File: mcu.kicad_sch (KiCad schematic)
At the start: 46 parts, among them J10 SWD, Cortex-M 10-pin 1.27 mm, Q20 2N7002, SW1 RESET (RUN to GND), SW2 BOOTSEL (via R24), U20 RP2354B, Y1 12 MHz ABM8-272-T3, CL 10 pF

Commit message: Schematic review: TPS2121 input stage, DS-009 ports, sequencing and CS fixes; docs trimmed
Datasheet-grounded review of the full flight-controller schematic. Downstream
of the input everything verified pin-by-pin (TPS62913, TPS7A20, RP2354B,
BMI088/BMP581/ADXL375, W25Q128, microSD, PWM). The 5 V input stage did not:

- LM66100 (5.5 V rec-op / 6 V abs-max) replaced by one TPS2121 mux (U25):
  BEC priority on IN1, OV lockout ~5.86 V, current limit ~1.5 A, reverse
  blocking on both inputs, source status on GPIO39. Input spec 4.75-5.5 V.
- 5V_IN: 2x4.7 uF + 100 uF + SMAJ5.0A TVS; J3 JST-XH -> XT30PW-M (pin 1 GND).
- J6/J7/J9 reordered to Pixhawk DS-009 (VCC/sig/sig/GND); GPS/ELRS VCC 5 V.
- VIN_SENSE 22k/10k (full scale 10.6 V, was saturating at 5.5 V).
- TPS7A20 EN <- PWR_GOOD so V3V3_ANA rises after V3V3_SYS.
- RP2354B VREG_AVDD moved to V3V3_SYS (datasheet 6.1.8: must power up with
  VREG_VIN); ADC_AVDD stays on V3V3_ANA.
- 10k pull-ups on the four sensor chip-selects.
- ERC "global label appears once" re-enabled (0 hits).

Generator, netlist checker and SPICE decks updated (TPS2121 behavioral model,
new over-voltage and 2S mis-plug corners). Build idempotent, 143 pin mappings
PASS, ERC 0/0, all corners PASS.

Docs: POWER_*.md history removed, rationale folded into DESIGN_SPEC Decisions;
808 -> 290 lines across README, DESIGN_SPEC, LIBRARIES, simulations/README.

Co-Authored-By: Claude Fable 5.1 <noreply@anthropic.com>
Claude-Session: https://claude.ai/code/session_015cFNiWgf35VN2T43HaK8PE
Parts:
- R27: value 10k / 1%, 5V_IN top -> 22k / 1%, 5V_IN top
- R28: value 15k / 1%, 5V_IN bottom -> 10k / 1%, 5V_IN bottom
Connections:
- net V3V3_ANA: no longer R20.1
- net V3V3_SYS: now also R20.1
- net PWR_SRC_ST: now reaches U20.48 (GPIO39)
- no-connect marks 13 -> 12
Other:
- note added: "Crystal circuit per design guide Sec 4: ABM8-272-T3, 15 pF each side (7.5 pF series + ~3 pF stray = 10.5 pF vs CL 10 pF), 1 k in the XOUT leg to limit drive with a 50 ohm ESR crystal. C38 is the single design-guide decoupling exception (pins 68+69 share it). VREG_AVDD RC = 33 ohm + 4.7 uF (design guide Sec 2.1), taken from V3V3_SYS; VREG_FB is tied to DVDD, VREG_PGND to GND, EP to GND."
- note added: "PORT NAMING: a port label is named for the peripheral pin it comes from, so GPS_TX / ELRS_TX are module outputs and land on MCU UART RX pins, while GPS_RX / ELRS_RX are module inputs fed by the MCU UART TX pins. On J6/J7 (POWER 3, Pixhawk DS-009 order 1 VCC / 2 TX / 3 RX / 4 GND) pin 2 is therefore GPS_RX / ELRS_RX. J6 and J7 VCC are on V5_SYS; J9 VCC stays on V3V3_SYS. All port SIGNAL pins remai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"
- note added: "RP2354B, QFN-80, 2 MB in-package QSPI flash. Digital rails on V3V3_SYS, core DVDD from the on-chip buck. RAIL SPLIT: V3V3_ANA (TPS7A20 LDO) now feeds exactly one RP2354B pin - ADC_AVDD (pin 59, with C40). The core regulator input filter R20/C41 that produces VREG_AVDD is fed from V3V3_SYS instead, so the buck-converter reference current no longer flows out of the low-noise analog rail and the sen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"
- note added: "Telemetry dividers, 100 nF at each ADC pin. VIN_SENSE (R27/R28 22k/10k) scales by 10/32 = 0.3125, so the 3.3 V ADC full scale is 10.56 V: 1.56 V at 5.00 V in, 1.72 V at 5.50 V, and a 2S mis-plug at 8.4 V still reads on-scale (2.63 V) instead of pinning the input, which is the point of the wider divider. VBUS_SENSE keeps 10k/15k. Buzzer runs from V5_SYS (avionics OR output), never from the servo b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"
- note removed: "Crystal circuit per design guide Sec 4: ABM8-272-T3, 15 pF each side (7.5 pF series + ~3 pF stray = 10.5 pF vs CL 10 pF), 1 k in the XOUT leg to limit drive with a 50 ohm ESR crystal. C38 is the single design-guide decoupling exception (pins 68+69 share it). VREG_AVDD RC = 33 ohm + 4.7 uF (design guide Sec 2.1); VREG_FB is tied to DVDD, VREG_PGND to GND, EP (pin 81) to GND."
- note removed: "PORT NAMING: a port label is named for the peripheral pin it comes from, so GPS_TX / ELRS_TX are module outputs and land on MCU UART RX pins, while GPS_RX / ELRS_RX are module inputs fed by the MCU UART TX pins. J6/J7/J9 (POWER 3) are 3.3 V logic powered directly from V3V3_SYS."
- note removed: "RP2354B, QFN-80, 2 MB in-package QSPI flash. Digital rails on V3V3_SYS, analog rails on V3V3_ANA, core DVDD from the on-chip buck. Decoupling, core regulator, crystal and BOOTSEL follow the RP2350 hardware design guide; every pin net is a global label."
- note removed: "Telemetry dividers: 10k/15k gives 3.00 V at 5.00 V in, 3.15 V at 5.25 V; 100 nF at each ADC pin. Buzzer runs from V5_SYS (avionics OR output), never from the servo bus; D22 clamps the coil kick. QSPI_* are the dedicated QSPI pads: they reach the in-package flash die AND the package pins (RP2350 datasheet Sec 14.3), so U24 shares the bus with GPIO0/QMI CS1n (FLASH_CS1) as its select. RP2354 requir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"

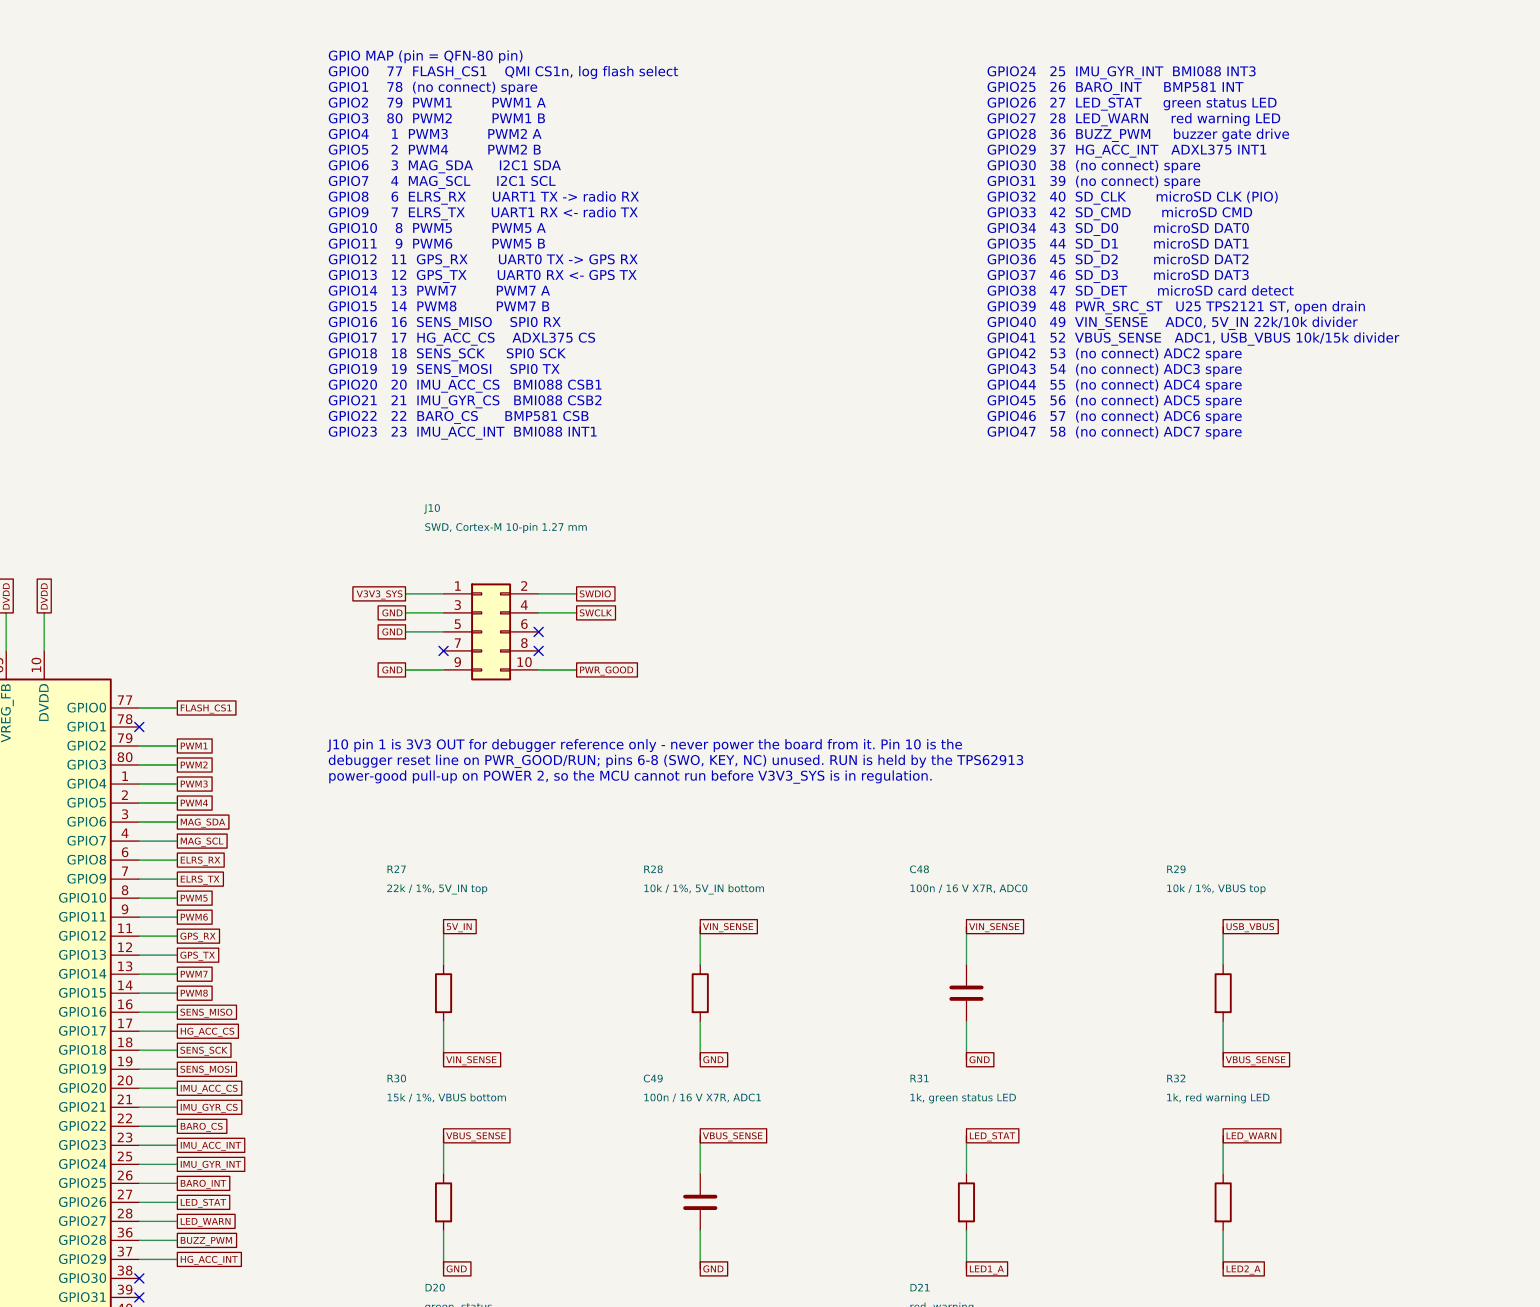
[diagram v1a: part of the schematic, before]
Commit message: Replace BMI088 with ICM-45686; vendor all footprints and 3D models for layout
Sensors: U21 is now the TDK ICM-45686 (single AP_CS on GPIO20 as IMU_CS,
INT1/INT2 on GPIO23/24, GPIO21 spare, R49 dropped, VDD+VDDIO on V3V3_ANA
with 100 nF + 1 uF each). Project-local symbol, footprint and stand-in STEP;
footprint numbering verified against DS-000577 Rev 1.0 Sec 11.2 (CCW, top
view). BMI088_SPI derived-symbol machinery removed from the generator.

Layout readiness: new tools/audit_footprints.py checks every component for
a resolvable footprint and present 3D model (128/128 OK). The seven official
KiCad footprints whose STEP files are absent from kicad-packages3d 10.0.6
are vendored into MARV_Packages.pretty with project-local models in
MARV_Packages.3dshapes: manufacturer STEPs (Coilcraft XGL4030, Molex
104031-0811), EasyEDA model (HRO TYPE-C-31-M-12), FreeCAD-generated bodies
from tools/3d/ (RP2354B QFN-80, TPS62913 RPU0010A, TPS2121 RUX0012A, Amass
XT30PW-M), and KiCad generic stand-ins (BMP581, ADXL375). Model offsets were
derived by measurement and confirmed in a rendered check board.
PROVENANCE.md records source, licence and SHA256 per model; LIBRARIES.md
lists the pre-fab 3D-viewer checks and the unverified dimensions.

Checks: build idempotent, ERC 0/0, check_power_netlist 149 mappings /
128 components, run_power_checks PASS, audit 0 needing action.

Co-Authored-By: Claude Fable 5.1 <noreply@anthropic.com>
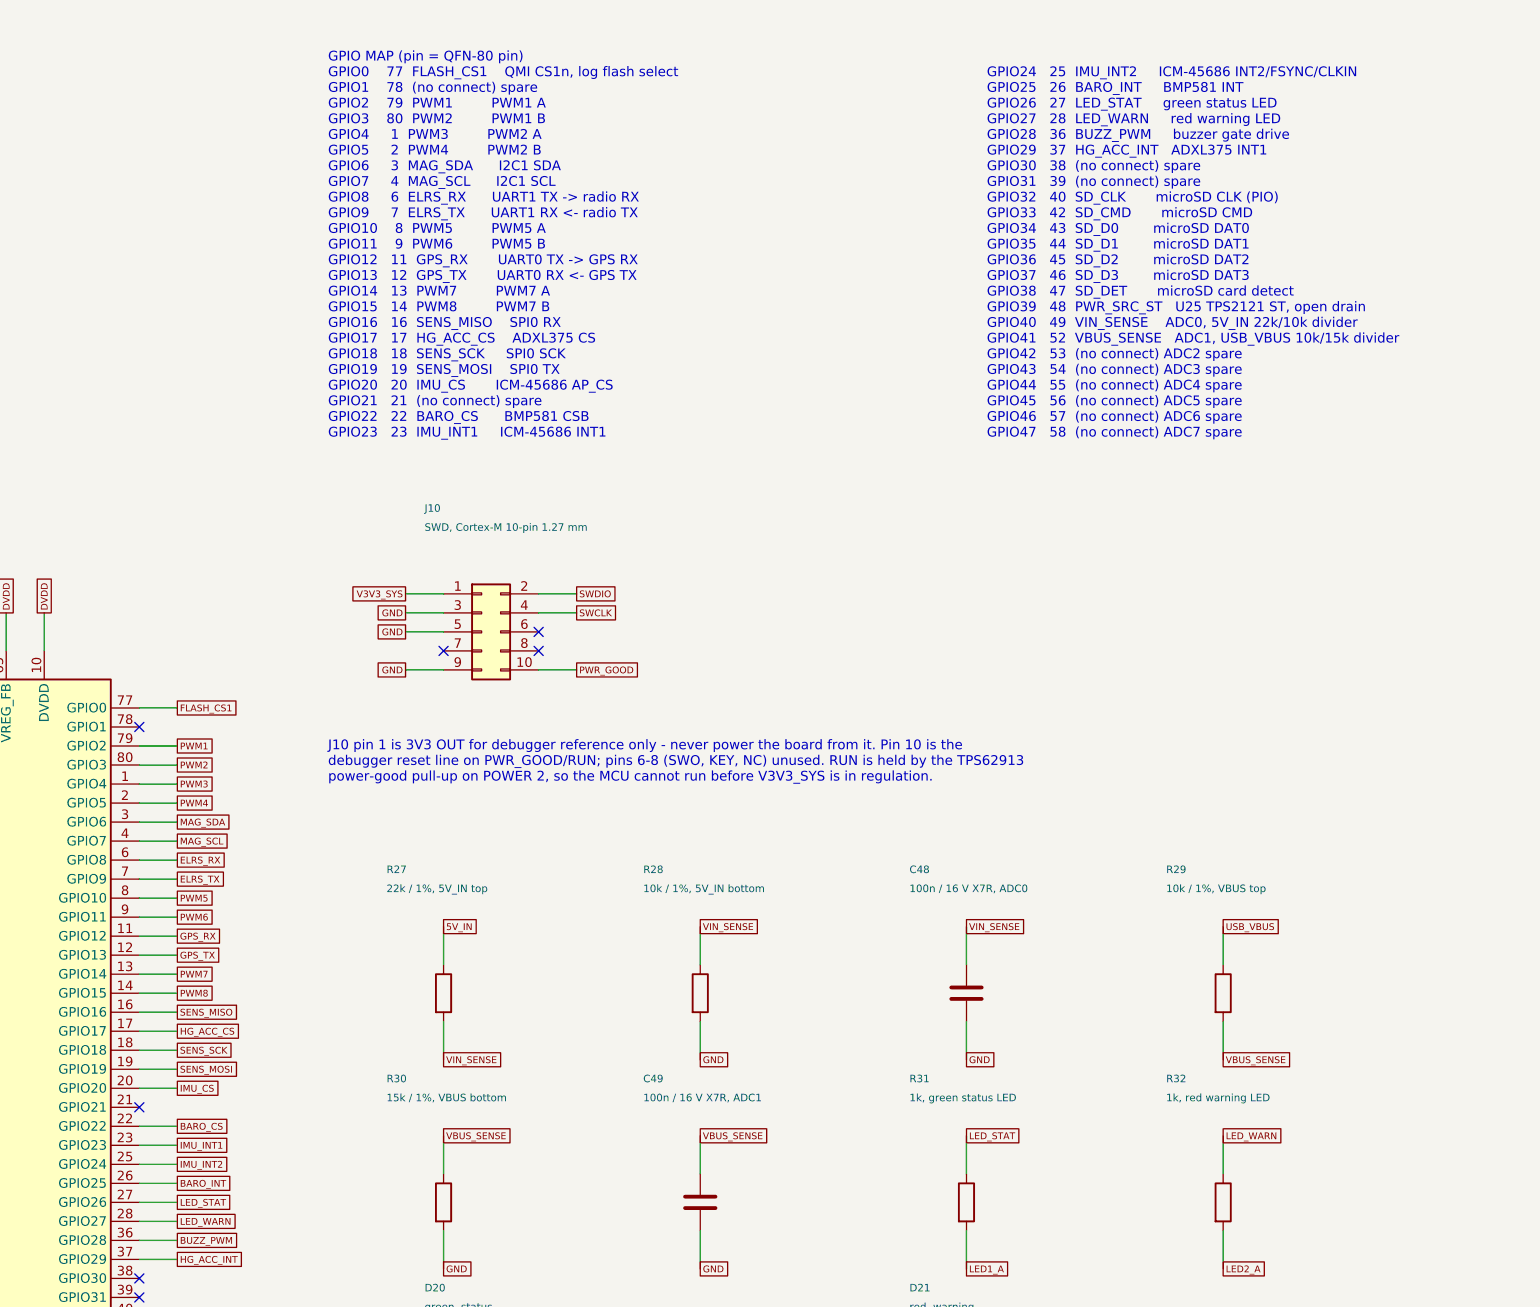
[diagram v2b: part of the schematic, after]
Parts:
- U20: footprint Package_DFN_QFN:QFN-80-1EP_10x10mm_P0.4mm_EP3.4x3.4mm -> MARV_Packages:QFN-80-1EP_10x10mm_P0.4mm_EP3.4x3.4mm
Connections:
- net IMU_ACC_CS renamed IMU_CS
- net IMU_ACC_INT renamed IMU_INT1
- net IMU_GYR_CS: no longer names the net of U20.21 (GPIO21)
- net IMU_GYR_INT renamed IMU_INT2
- no-connect marks 12 -> 13
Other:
- note added: "GPIO24 25 IMU_INT2 ICM-45686 INT2/FSYNC/CLKIN GPIO25 26 BARO_INT BMP581 INT GPIO26 27 LED_STAT green status LED GPIO27 28 LED_WARN red warning LED GPIO28 36 BUZZ_PWM buzzer gate drive GPIO29 37 HG_ACC_INT ADXL375 INT1 GPIO30 38 (no connect) spare GPIO31 39 (no connect) spare GPIO32 40 SD_CLK microSD CLK (PIO) GPIO33 42 SD_CMD microSD CMD GPIO34 43 SD_D0 microSD DAT0 GPIO35 44 SD_D1 microSD DAT1 G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"
- note removed: "GPIO24 25 IMU_GYR_INT BMI088 INT3 GPIO25 26 BARO_INT BMP581 INT GPIO26 27 LED_STAT green status LED GPIO27 28 LED_WARN red warning LED GPIO28 36 BUZZ_PWM buzzer gate drive GPIO29 37 HG_ACC_INT ADXL375 INT1 GPIO30 38 (no connect) spare GPIO31 39 (no connect) spare GPIO32 40 SD_CLK microSD CLK (PIO) GPIO33 42 SD_CMD microSD CMD GPIO34 43 SD_D0 microSD DAT0 GPIO35 44 SD_D1 microSD DAT1 GPIO36 45 SD_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"
